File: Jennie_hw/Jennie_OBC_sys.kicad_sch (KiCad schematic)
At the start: 28 parts, among them IC1 TPS79533DCQ, J5 Conn_01x10, J6 Conn_01x15, SW2 SW_MEC_5E, SW3 SW_MEC_5E, U1 ATmega328PB-A, Y1 16MHz

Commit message: remove before start switch added
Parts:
- added J2: Barrel_Jack_Switch, Connector_BarrelJack:BarrelJack_Horizontal, symbol Connector:Barrel_Jack_Switch
- SW2: value SW_MEC_5E -> (none)
- U2: value ~ -> TP4056 charger module
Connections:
- net GND: now also J2.1
- net V_OUT: now also J2.2; no longer U2.3 (OUT+)
- new net OUT+: J2.3, U2.3 (OUT+)
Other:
- note added: "Basic I/O"
- note added: "Batt. connector"
- note added: "Batt. volateg meas."
- note added: "Charger moduel for battery"
- note added: "Crystal for MCU"
- note added: "Decoupling caps"
- note added: "LDO (from Vbatt to 3.3V)"
- note added: "Max Iout: 3A"
- note added: "RBF switch"
- note added: "Reset btn for MCU"
- moved on the sheet: C2, C3, C4, C5, D1, IC1, J1, J5, J6, R1, R2, R6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

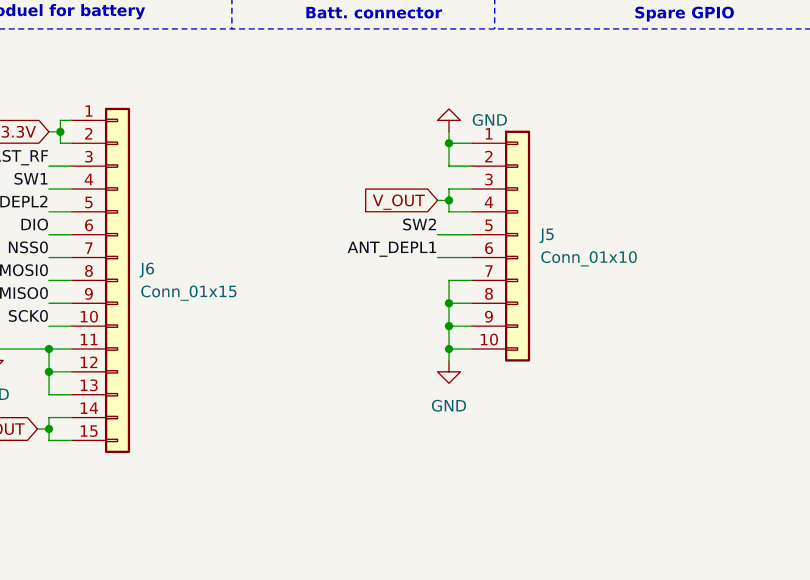
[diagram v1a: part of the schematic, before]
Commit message: small fix of small routing error on Jennie PCB (V_batt routed to different pins on pinheader to maintain compatibility with Jára pinheader)
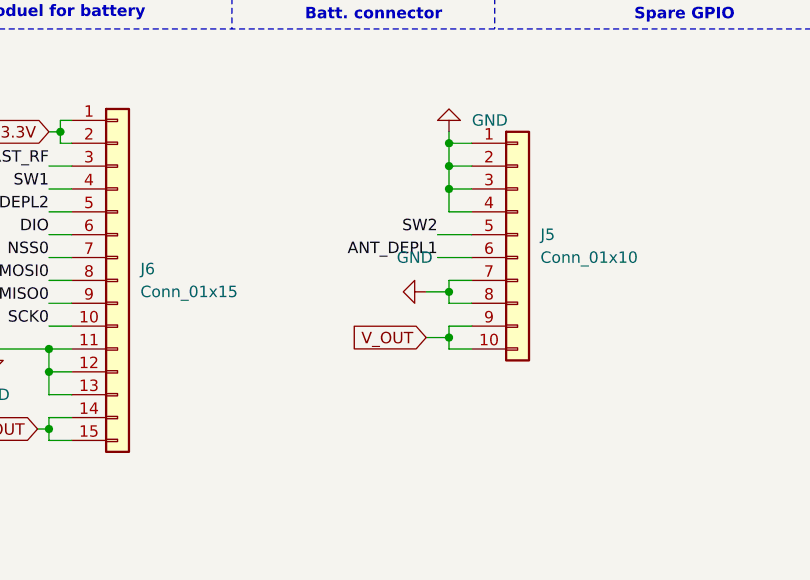
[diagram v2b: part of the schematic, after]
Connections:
- net GND: now also J5.3 (Pin_3), J5.4 (Pin_4); no longer J5.10 (Pin_10), J5.9 (Pin_9)
- net V_OUT: now also J5.10 (Pin_10), J5.9 (Pin_9); no longer J5.3 (Pin_3), J5.4 (Pin_4)
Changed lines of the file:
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@@
 	)
 	(junction
-		(at 186.69 130.81)
-		(diameter 0)
-		(color 0 0 0 0)
-	)
-	(junction
 		(at 186.69 113.03)
 		(diameter 0)
@@
 	)
 	(junction
-		(at 186.69 135.89)
-		(diameter 0)
-		(color 0 0 0 0)
-	)
-	(junction
 		(at 142.24 144.78)
 		(diameter 0)
@@
 	)
 	(junction
-		(at 186.69 119.38)
+		(at 186.69 118.11)
 		(diameter 0)
 		(color 0 0 0 0)
@@
 	)
 	(junction
-		(at 48.26 31.75)
+		(at 186.69 129.54)
 		(diameter 0)
 		(color 0 0 0 0)
 	)
 	(junction
-		(at 186.69 133.35)
+		(at 48.26 31.75)
 		(diameter 0)
 		(color 0 0 0 0)
@@
 	)
 	(junction
+		(at 186.69 134.62)
+		(diameter 0)
+		(color 0 0 0 0)
+	)
+	(junction
+		(at 186.69 115.57)
+		(diameter 0)
+		(color 0 0 0 0)
+	)
+	(junction
 		(at 261.62 39.37)
 		(diameter 0)
@@
 	(wire
 		(pts
-			(xy 189.23 133.35) (xy 186.69 133.35)
-		)
-		(stroke
-			(width 0)
-			(type default)
-		)
-	)
-	(wire
-		(pts
 			(xy 246.38 39.37) (xy 246.38 40.64)
 		)
@@
 	(wire
 		(pts
-			(xy 92.71 81.28) (xy 95.25 81.28)
+			(xy 186.69 133.35) (xy 186.69 134.62)
 		)
 		(stroke
@@
 	(wire
 		(pts
-			(xy 36.83 31.75) (xy 36.83 35.56)
-		)
-		(stroke
-			(width 0)
-			(type default)
-		)
-	)
-	(wire
-		(pts
-			(xy 264.16 69.85) (xy 264.16 72.39)
+			(xy 92.71 81.28) (xy 95.25 81.28)
 		)
 		(stroke
@@
 	(wire
 		(pts
-			(xy 71.12 167.64) (xy 67.31 167.64)
+			(xy 36.83 31.75) (xy 36.83 35.56)
 		)
 		(stroke
@@
 	(wire
 		(pts
-			(xy 186.69 135.89) (xy 186.69 137.16)
+			(xy 264.16 69.85) (xy 264.16 72.39)
 		)
 		(stroke
@@
 	(wire
 		(pts
-			(xy 186.69 135.89) (xy 189.23 135.89)
+			(xy 71.12 167.64) (xy 67.31 167.64)
 		)
 		(stroke
@@
 	(wire
 		(pts
-			(xy 186.69 120.65) (xy 189.23 120.65)
-		)
-		(stroke
-			(width 0)
-			(type default)
-		)
-	)
-	(wire
-		(pts
 			(xy 124.46 34.29) (xy 135.89 34.29)
 		)
@@
 	(wire
 		(pts
+			(xy 186.69 120.65) (xy 186.69 118.11)
+		)
+		(stroke
+			(width 0)
+			(type default)
+		)
+	)
+	(wire
+		(pts
 			(xy 215.9 40.64) (xy 215.9 43.18)
 		)
@@
 	(wire
 		(pts
-			(xy 185.42 119.38) (xy 186.69 119.38)
-		)
-		(stroke
-			(width 0)
-			(type default)
-		)
-	)
-	(wire
-		(pts
-			(xy 186.69 133.35) (xy 186.69 135.89)
-		)
-		(stroke
-			(width 0)
-			(type default)
-		)
-	)
-	(wire
-		(pts
 			(xy 142.24 138.43) (xy 142.24 140.97)
 		)
@@
 	(wire
 		(pts
-			(xy 149.86 83.82) (xy 149.86 86.36)
+			(xy 186.69 134.62) (xy 186.69 135.89)
 		)
 		(stroke
@@
 	(wire
 		(pts
-			(xy 53.34 106.68) (xy 53.34 107.95)
+			(xy 149.86 83.82) (xy 149.86 86.36)
 		)
 		(stroke
@@
 	(wire
 		(pts
-			(xy 186.69 128.27) (xy 186.69 130.81)
+			(xy 53.34 106.68) (xy 53.34 107.95)
 		)
 		(stroke
@@
 		)
 	)
-	(polyline
+	(wire
 		(pts
-			(xy 191.77 19.05) (xy 191.77 100.33)
+			(xy 186.69 128.27) (xy 186.69 129.54)
 		)
 		(stroke
 			(width 0)
-			(type dash)
+			(type default)
 		)
 	)
 	(wire
 		(pts
-			(xy 186.69 118.11) (xy 186.69 119.38)
+			(xy 186.69 118.11) (xy 186.69 115.57)
 		)
 		(stroke
@@
 		)
 	)
-	(wire
+	(polyline
 		(pts
-			(xy 210.82 80.01) (xy 212.09 80.01)
+			(xy 191.77 19.05) (xy 191.77 100.33)
 		)
 		(stroke
 			(width 0)
-			(type default)
+			(type dash)
 		)
 	)
 	(wire
 		(pts
-			(xy 86.36 147.32) (xy 90.17 147.32)
+			(xy 210.82 80.01) (xy 212.09 80.01)
 		)
 		(stroke
@@
 	(wire
 		(pts
-			(xy 245.11 69.85) (xy 245.11 71.12)
+			(xy 86.36 147.32) (xy 90.17 147.32)
 		)
 		(stroke
@@
 	(wire
 		(pts
-			(xy 71.12 49.53) (xy 71.12 48.26)
+			(xy 245.11 69.85) (xy 245.11 71.12)
 		)
 		(stroke
@@
 	(wire
 		(pts
-			(xy 186.69 130.81) (xy 186.69 133.35)
+			(xy 71.12 49.53) (xy 71.12 48.26)
 		)
 		(stroke
@@
 	(wire
 		(pts
-			(xy 186.69 118.11) (xy 189.23 118.11)
+			(xy 186.69 129.54) (xy 186.69 130.81)
 		)
 		(stroke
@@
 	(wire
 		(pts
+			(xy 186.69 118.11) (xy 189.23 118.11)
+		)
+		(stroke
+			(width 0)
+			(type default)
+		)
+	)
+	(wire
+		(pts
 			(xy 67.31 127) (xy 71.12 127)
 		)
@@
 	(wire
 		(pts
+			(xy 184.15 129.54) (xy 186.69 129.54)
+		)
+		(stroke
+			(width 0)
+			(type default)
+		)
+	)
+	(wire
+		(pts
 			(xy 215.9 40.64) (xy 220.98 40.64)
 		)
@@
 	(wire
 		(pts
+			(xy 189.23 120.65) (xy 186.69 120.65)
+		)
+		(stroke
+			(width 0)
+			(type default)
+		)
+	)
+	(wire
+		(pts
 			(xy 144.78 128.27) (xy 142.24 128.27)
 		)
@@
 	(wire
 		(pts
+			(xy 186.69 133.35) (xy 189.23 133.35)
+		)
+		(stroke
+			(width 0)
+			(type default)
+		)
+	)
+	(wire
+		(pts
 			(xy 54.61 31.75) (xy 54.61 35.56)
 		)
@@
 	(wire
 		(pts
+			(xy 186.69 135.89) (xy 189.23 135.89)
+		)
+		(stroke
+			(width 0)
+			(type default)
+		)
+	)
+	(wire
+		(pts
 			(xy 179.07 82.55) (xy 179.07 87.63)
 		)
@@
 		)
 	)
+	(wire
+		(pts
+			(xy 184.15 134.62) (xy 186.69 134.62)
+		)
+		(stroke
+			(width 0)
+			(type default)
+		)
+	)
 	(polyline
 		(pts
@@
 	(wire
 		(pts
-			(xy 186.69 119.38) (xy 186.69 120.65)
-		)
-		(stroke
-			(width 0)
-			(type default)
-		)
-	)
-	(wire
-		(pts
 			(xy 52.07 107.95) (xy 52.07 109.22)
 		)
@@
 	(global_label "V_OUT"
 		(shape input)
-		(at 185.42 119.38 180)
+		(at 184.15 134.62 180)
 		(fields_autoplaced yes)
 		(effects
@@
 		)
 		(property "Intersheetrefs" "${INTERSHEET_REFS}"
-			(at 176.75 119.38 0)
+			(at 175.48 134.62 0)
 			(effects
 				(font
@@
 	(symbol
 		(lib_id "power:GND")
-		(at 186.69 137.16 0)
+		(at 184.15 129.54 270)
 		(unit 1)
 		(exclude_from_sim no)
@@
 		(fields_autoplaced yes)
 		(property "Reference" "#PWR024"
-			(at 186.69 143.51 0)
+			(at 177.8 129.54 0)
 			(effects
 				(font
@@
 		)
 		(property "Value" "GND"
-			(at 186.69 142.24 0)
+			(at 182.88 125.73 90)
 			(effects
 				(font
@@
 		)
 		(property "Footprint" ""
-			(at 186.69 137.16 0)
+			(at 184.15 129.54 0)
 			(effects
 				(font
@@
 		)
 		(property "Datasheet" ""
-			(at 186.69 137.16 0)
+			(at 184.15 129.54 0)
 			(effects
 				(font
@@
 		)
 		(property "Description" "Power symbol creates a global label with name \"GND\" , ground"
-			(at 186.69 137.16 0)
+			(at 184.15 129.54 0)
 			(effects
 				(font
